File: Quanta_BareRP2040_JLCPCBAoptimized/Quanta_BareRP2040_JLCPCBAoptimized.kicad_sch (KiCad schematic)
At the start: 252 parts, among them J1 USB_C_Receptacle_USB2.0, J10 Conn_01x05_Socket GPIOs, J2 Conn_01x02_Socket VBUS 5V, J3 Conn_01x02_Socket 3V3, J4 ~{BOOTSEL}, J5 Conn_01x04_Socket SWD, J6 USB_A_Receptacle_UBS2.0, J7 USB_C_Receptacle_USB2.0, J8 Conn_01x04_Socket I2C display, J9 USB_C_Receptacle_USB2.0, SW1 SW_Push, SW10 SW_Push, SW11 SW_Push, SW12 SW_Push, SW13 SW_Push, SW14 SW_Push, SW15 SW_Push, SW16 SW_Push, SW17 SW_Push, SW18 SW_Push, SW19 SW_Push, SW2 SW_Push, SW20 SW_Push, SW21 SW_Push, SW22 SW_Push, SW23 SW_Push, SW24 SW_Push, SW25 SW_Push, SW26 SW_Push, SW27 SW_Push, SW28 SW_Push, SW29 SW_Push, SW3 SW_Push, SW30 SW_Push, SW31 SW_Push, SW32 SW_Push, SW33 SW_Push, SW34 SW_Push, SW35 SW_Push, SW36 SW_Push, SW37 SW_Push, SW38 SW_Push, SW39 SW_Push, SW4 SW_Push, SW40 SW_Push, SW41 SW_Push, SW42 SW_Push, SW43 SW_Push, SW44 SW_Push, SW45 SW_Push, SW46 SW_Push, SW47 SW_Push, SW48 SW_Push, SW49 SW_Push, SW5 SW_Push, SW50 SW_Push, SW51 SW_Push, SW52 SW_Push, SW53 SW_Push, SW54 SW_Push, SW55 SW_Push, SW56 SW_Push, SW57 SW_Push, SW58 SW_Push, SW59 SW_Push, SW6 SW_Push, SW60 SW_Push, SW61 SW_Push, SW62 SW_Push, SW63 SW_Push, SW64 SW_Push, SW65 SW_Push, SW66 SW_Push, SW67 SW_Push, SW68 SW_Push, SW69 SW_Push, SW7 SW_Push, SW70 SW_Push, SW71 SW_Push, SW72 SW_Push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

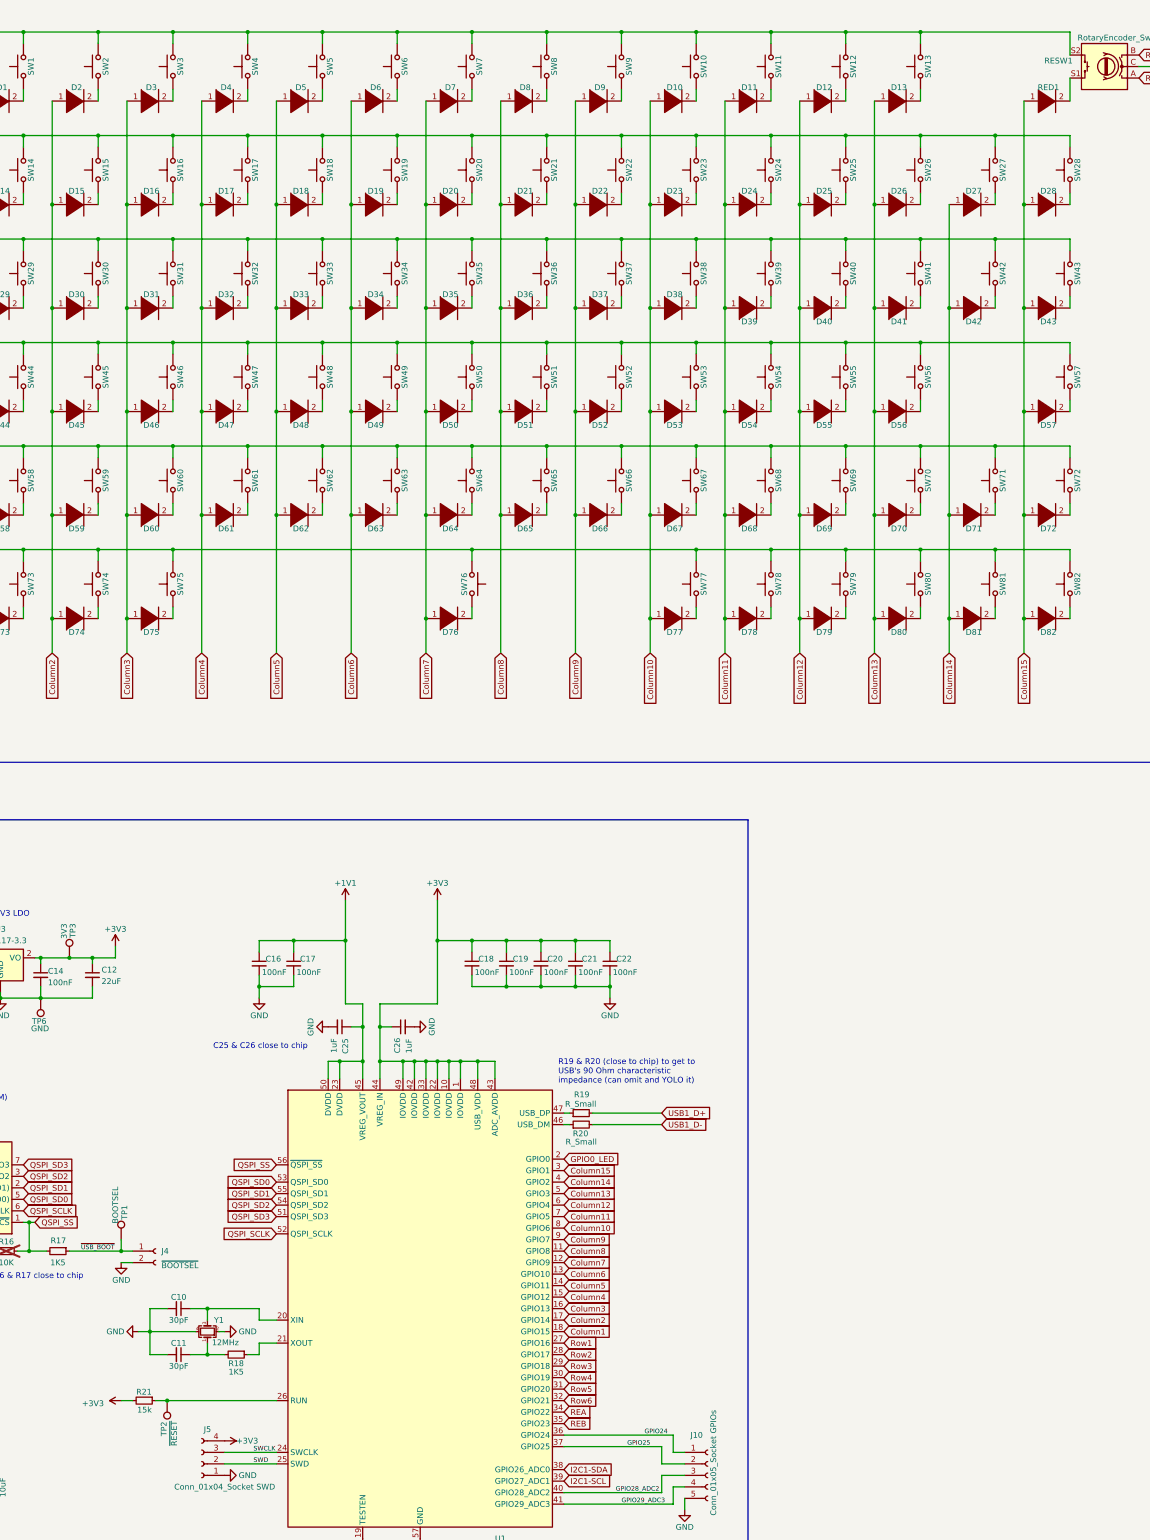
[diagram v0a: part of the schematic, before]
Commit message: add spst switch to bare rp2040 schematic
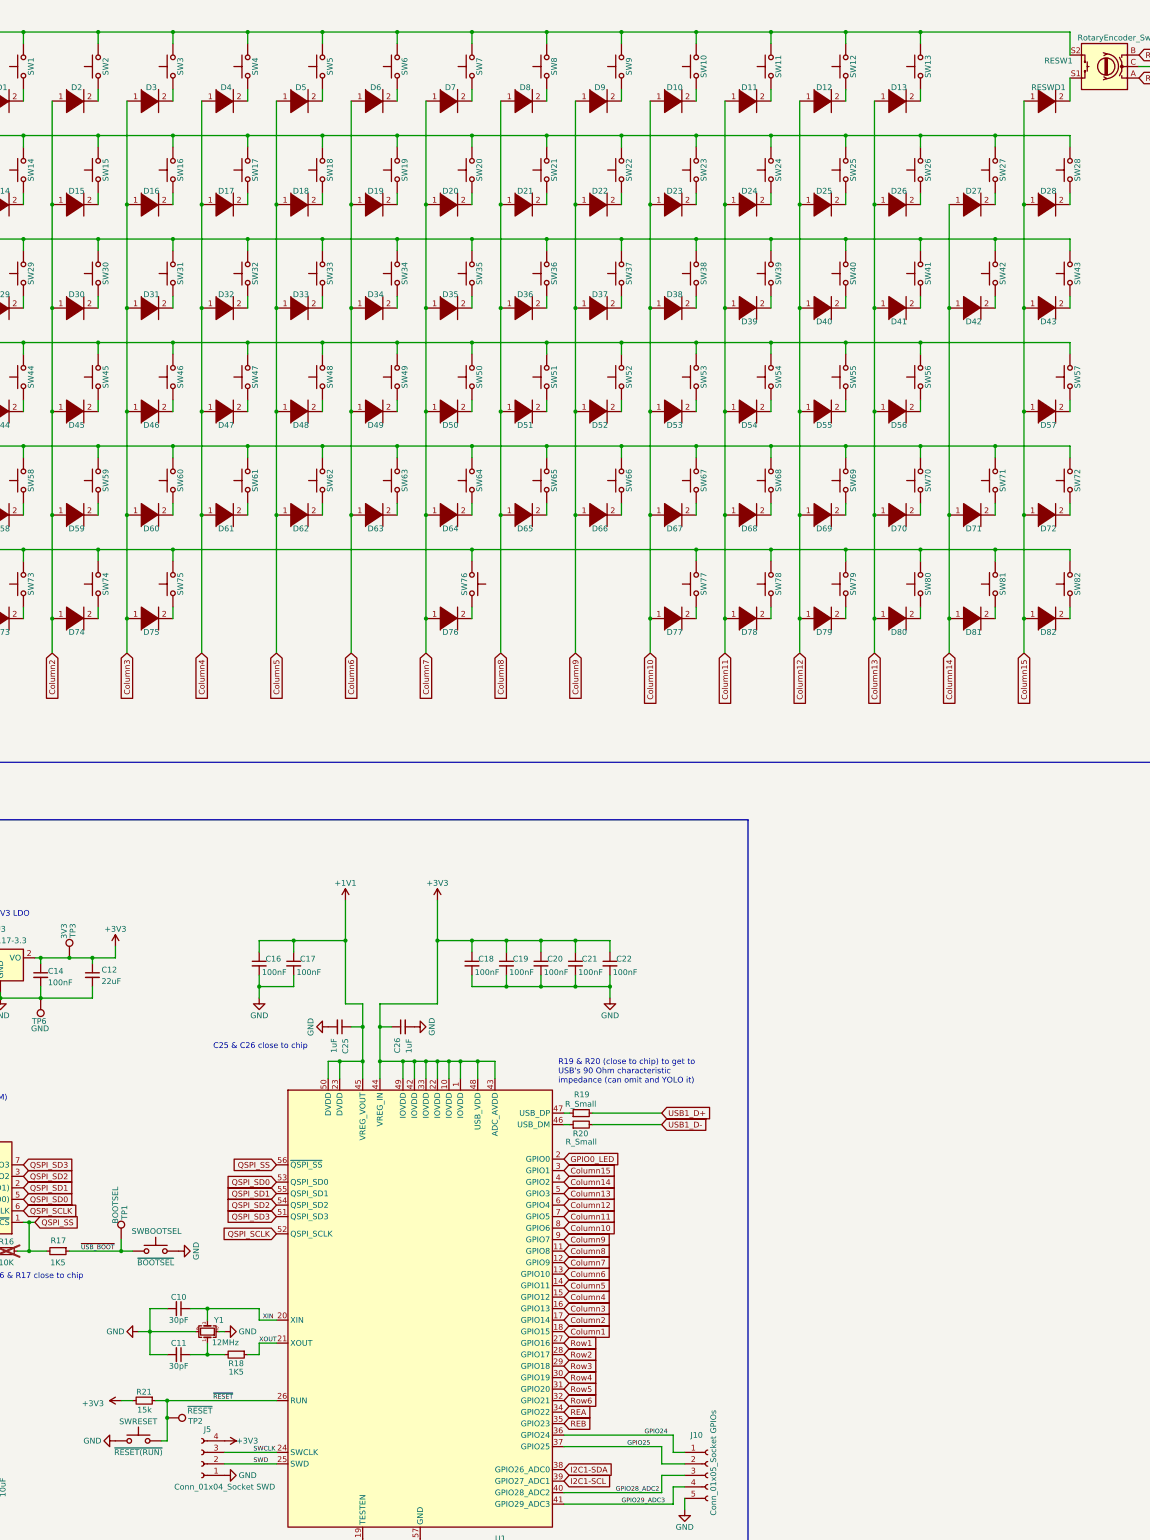
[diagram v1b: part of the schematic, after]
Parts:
- removed J4: ~{BOOTSEL}, Connector_PinHeader_2.54mm:PinHeader_1x02_P2.54mm_Vertical, symbol Connector:Conn_01x02_Socket
- added SWBOOTSEL: ~{BOOTSEL}, Button_Switch_SMD:SW_Push_1P1T_XKB_TS-1187A, symbol Switch:SW_Push
- added SWRESET: ~{RESET(RUN)}, Button_Switch_SMD:SW_Push_1P1T_XKB_TS-1187A, symbol Switch:SW_Push
- renumbered RED1 to RESWD1
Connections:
- net GND: now also SWBOOTSEL.2, SWRESET.1
- net ~{USB_BOOT}: now also SWBOOTSEL.1
- net XIN: now reaches C10.1, U1.20 (XIN), Y1.3
- net XOUT: now reaches R18.1, U1.21 (XOUT)
- net ~{RESET}: now reaches R21.1, TP2.1, U1.26 (RUN)
- net ~{RESET}: now also SWRESET.2
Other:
- moved on the sheet: TP2
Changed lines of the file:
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@@
     (title "Quanta Keyboard Schematic Bare (RP2040 JLCPCBA)")
     (date "2023-06-11")
-    (rev "2.2")
+    (rev "3.0")
     (company "0bsilab")
     (comment 1 "by Lucas Placentino")
@@
   (junction (at 254 124.46) (diameter 0) (color 0 0 0 0)
   )
+  (junction (at 97.79 346.71) (diameter 0) (color 0 0 0 0)
+  )
   (junction (at 154.94 78.74) (diameter 0) (color 0 0 0 0)
   )
@@
     (stroke (width 0) (type default))
   )
+  (wire (pts (xy 97.79 346.71) (xy 97.79 351.79))
+    (stroke (width 0) (type default))
+  )
   (wire (pts (xy 106.68 332.74) (xy 110.49 332.74))
     (stroke (width 0) (type default))
@@
     (stroke (width 0) (type default))
   )
+  (wire (pts (xy 106.68 322.58) (xy 118.11 322.58))
+    (stroke (width 0) (type default))
+  )
   (wire (pts (xy 66.04 303.53) (xy 67.31 303.53))
     (stroke (width 0) (type default))
@@
     (stroke (width 0) (type default))
   )
+  (wire (pts (xy 97.79 346.71) (xy 97.79 342.9))
+    (stroke (width 0) (type default))
+  )
   (wire (pts (xy 82.55 63.5) (xy 99.06 63.5))
     (stroke (width 0) (type default))
@@
     (stroke (width 0) (type default))
   )
-  (wire (pts (xy 106.68 322.58) (xy 118.11 322.58))
-    (stroke (width 0) (type default))
-  )
   (wire (pts (xy 280.67 154.94) (xy 297.18 154.94))
     (stroke (width 0) (type default))
@@
     (stroke (width 0) (type default))
   )
+  (wire (pts (xy 97.79 351.79) (xy 96.52 351.79))
+    (stroke (width 0) (type default))
+  )
   (wire (pts (xy 148.59 132.08) (xy 165.1 132.08))
     (stroke (width 0) (type default))
@@
     (stroke (width 0) (type default))
   )
-  (wire (pts (xy 90.17 312.42) (xy 87.63 312.42))
-    (stroke (width 0) (type default))
-  )
   (wire (pts (xy 39.37 252.73) (xy 39.37 254))
     (stroke (width 0) (type default))
@@
     (effects (font (size 1 1)) (justify left bottom))
   )
+  (label "XIN" (at 118.9133 325.12 0) (fields_autoplaced)
+    (effects (font (size 1 1)) (justify left bottom))
+  )
   (label "GPIO28_ADC2" (at 196.85 363.22 0) (fields_autoplaced)
     (effects (font (size 1 1)) (justify left bottom))
@@
     (effects (font (size 1 1)) (justify left bottom))
   )
+  (label "XOUT" (at 118.11 330.2 0) (fields_autoplaced)
+    (effects (font (size 1 1)) (justify left bottom))
+  )
+  (label "~{RESET}" (at 107.95 342.9 0) (fields_autoplaced)
+    (effects (font (size 1 1)) (justify left bottom))
+  )
   (label "USB2-" (at 415.29 156.21 0) (fields_autoplaced)
     (effects (font (size 1.27 1.27)) (justify left bottom))
@@
     )
   )
+  (symbol (lib_id "Switch:SW_Push") (at 95.25 309.88 0) (unit 1)
+    (in_bom yes) (on_board yes) (dnp no)
+    (property "Reference" "SWBOOTSEL" (at 95.4399 305.4889 0)
+      (effects (font (size 1.27 1.27)))
+    )
+    (property "Value" "~{BOOTSEL}" (at 95.25 312.42 0)
+      (effects (font (size 1.27 1.27)))
+    )
+    (property "Footprint" "Button_Switch_SMD:SW_Push_1P1T_XKB_TS-1187A" (at 95.25 304.8 0)
+      (effects (font (size 1.27 1.27)) hide)
+    )
+    (property "Datasheet" "~" (at 95.25 304.8 0)
+      (effects (font (size 1.27 1.27)) hide)
+    )
+    (property "JLCPCB" "C318884" (at 95.25 309.88 0)
+      (effects (font (size 1.27 1.27)) hide)
+    )
+    (pin "1")
+    (pin "2")
+    (instances
+      (project "Quanta_BareRP2040_JLCPCBAoptimized"
+        (path "/0cabb2e6-4a46-4ffe-8ff7-d51fc1f6dda5"
+          (reference "SWBOOTSEL") (unit 1)
+        )
+      )
+    )
+  )
   (symbol (lib_id "power:GND") (at 455.93 46.99 90) (unit 1)
     (in_bom yes) (on_board yes) (dnp no)
@@
     )
   )
-  (symbol (lib_id "Connector:Conn_01x02_Socket") (at 95.25 309.88 0) (unit 1)
-    (in_bom yes) (on_board yes) (dnp no) (fields_autoplaced)
-    (property "Reference" "J4" (at 96.52 309.88 0)
-      (effects (font (size 1.27 1.27)) (justify left))
-    )
-    (property "Value" "~{BOOTSEL}" (at 96.52 313.055 0)
-      (effects (font (size 1.27 1.27)) (justify left))
-    )
-    (property "Footprint" "Connector_PinHeader_2.54mm:PinHeader_1x02_P2.54mm_Vertical" (at 95.25 309.88 0)
-      (effects (font (size 1.27 1.27)) hide)
-    )
-    (property "Datasheet" "~" (at 95.25 309.88 0)
-      (effects (font (size 1.27 1.27)) hide)
-    )
-    (pin "1")
-    (pin "2")
-    (instances
-      (project "Quanta_BareRP2040_JLCPCBAoptimized"
-        (path "/0cabb2e6-4a46-4ffe-8ff7-d51fc1f6dda5"
-          (reference "J4") (unit 1)
-        )
-      )
-    )
-  )
   (symbol (lib_name "SW_Push_1") (lib_id "Switch:SW_Push") (at 148.59 93.98 90) (unit 1)
     (in_bom yes) (on_board yes) (dnp no)
@@
     )
   )
+  (symbol (lib_id "power:GND") (at 86.36 351.79 270) (unit 1)
+    (in_bom yes) (on_board yes) (dnp no)
+    (property "Reference" "#PWR033" (at 80.01 351.79 0)
+      (effects (font (size 1.27 1.27)) hide)
+    )
+    (property "Value" "GND" (at 81.28 351.79 90)
+      (effects (font (size 1.27 1.27)))
+    )
+    (property "Footprint" "" (at 86.36 351.79 0)
+      (effects (font (size 1.27 1.27)) hide)
+    )
+    (property "Datasheet" "" (at 86.36 351.79 0)
+      (effects (font (size 1.27 1.27)) hide)
+    )
+    (pin "1")
+    (instances
+      (project "Quanta_BareRP2040_JLCPCBAoptimized"
+        (path "/0cabb2e6-4a46-4ffe-8ff7-d51fc1f6dda5"
+          (reference "#PWR033") (unit 1)
+        )
+      )
+    )
+  )
   (symbol (lib_id "pspice:DIODE") (at 93.98 55.88 0) (unit 1)
     (in_bom yes) (on_board yes) (dnp no)
@@
     )
   )
-  (symbol (lib_id "power:GND") (at 87.63 312.42 0) (unit 1)
+  (symbol (lib_id "power:GND") (at 100.33 309.88 90) (unit 1)
     (in_bom yes) (on_board yes) (dnp no)
-    (property "Reference" "#PWR052" (at 87.63 318.77 0)
+    (property "Reference" "#PWR052" (at 106.68 309.88 0)
       (effects (font (size 1.27 1.27)) hide)
     )
-    (property "Value" "GND" (at 89.6559 316.2788 0)
+    (property "Value" "GND" (at 104.1888 307.8541 0)
       (effects (font (size 1.27 1.27)) (justify right))
     )
-    (property "Footprint" "" (at 87.63 312.42 0)
+    (property "Footprint" "" (at 100.33 309.88 0)
       (effects (font (size 1.27 1.27)) hide)
     )
-    (property "Datasheet" "" (at 87.63 312.42 0)
+    (property "Datasheet" "" (at 100.33 309.88 0)
       (effects (font (size 1.27 1.27)) hide)
     )
@@
   (symbol (lib_id "pspice:DIODE") (at 292.1 55.88 0) (unit 1)
     (in_bom yes) (on_board yes) (dnp no)
-    (property "Reference" "RED1" (at 292.4253 52.8798 0)
+    (property "Reference" "RESWD1" (at 292.4253 52.8798 0)
       (effects (font (size 1.27 1.27)))
     )
@@
       (project "Quanta_BareRP2040_JLCPCBAoptimized"
         (path "/0cabb2e6-4a46-4ffe-8ff7-d51fc1f6dda5"
-          (reference "RED1") (unit 1)
+          (reference "RESWD1") (unit 1)
         )
       )
@@
     )
   )
+  (symbol (lib_id "Switch:SW_Push") (at 91.44 351.79 0) (unit 1)
+    (in_bom yes) (on_board yes) (dnp no)
+    (property "Reference" "SWRESET" (at 91.3964 347.5239 0)
+      (effects (font (size 1.27 1.27)))
+    )
+    (property "Value" "~{RESET(RUN)}" (at 91.44 354.33 0)
+      (effects (font (size 1.27 1.27)))
+    )
+    (property "Footprint" "Button_Switch_SMD:SW_Push_1P1T_XKB_TS-1187A" (at 91.44 346.71 0)
+      (effects (font (size 1.27 1.27)) hide)
+    )
+    (property "Datasheet" "~" (at 91.44 346.71 0)
+      (effects (font (size 1.27 1.27)) hide)
+    )
+    (property "JLCPCB" "C318884" (at 91.44 351.79 0)
+      (effects (font (size 1.27 1.27)) hide)
+    )
+    (pin "1")
+    (pin "2")
+    (instances
+      (project "Quanta_BareRP2040_JLCPCBAoptimized"
+        (path "/0cabb2e6-4a46-4ffe-8ff7-d51fc1f6dda5"
+          (reference "SWRESET") (unit 1)
+        )
+      )
+    )
+  )
   (symbol (lib_id "power:GND") (at 153.67 373.38 0) (unit 1)
     (in_bom yes) (on_board yes) (dnp no)
@@
     )
   )
-  (symbol (lib_id "Connector:TestPoint") (at 97.79 342.9 180) (unit 1)
+  (symbol (lib_id "Connector:TestPoint") (at 97.79 346.71 270) (unit 1)
     (in_bom yes) (on_board yes) (dnp no)
-    (property "Reference" "TP2" (at 97.0664 349.1405 90)
+    (property "Reference" "TP2" (at 104.0305 347.4336 90)
       (effects (font (size 1.27 1.27)))
     )
-    (property "Value" "~{RESET}" (at 99.3483 350.1431 90)
+    (property "Value" "~{RESET}" (at 105.0331 345.1517 90)
       (effects (font (size 1.27 1.27)))
     )
-    (property "Footprint" "TestPoint:TestPoint_Pad_D1.5mm" (at 92.71 342.9 0)
+    (property "Footprint" "TestPoint:TestPoint_Pad_D1.5mm" (at 97.79 351.79 0)
       (effects (font (size 1.27 1.27)) hide)
     )
-    (property "Datasheet" "~" (at 92.71 342.9 0)
+    (property "Datasheet" "~" (at 97.79 351.79 0)
       (effects (font (size 1.27 1.27)) hide)
     )
